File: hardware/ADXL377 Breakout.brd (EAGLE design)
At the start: 17.8 x 17.8 mm, 13 parts, among them U1 ADXL377

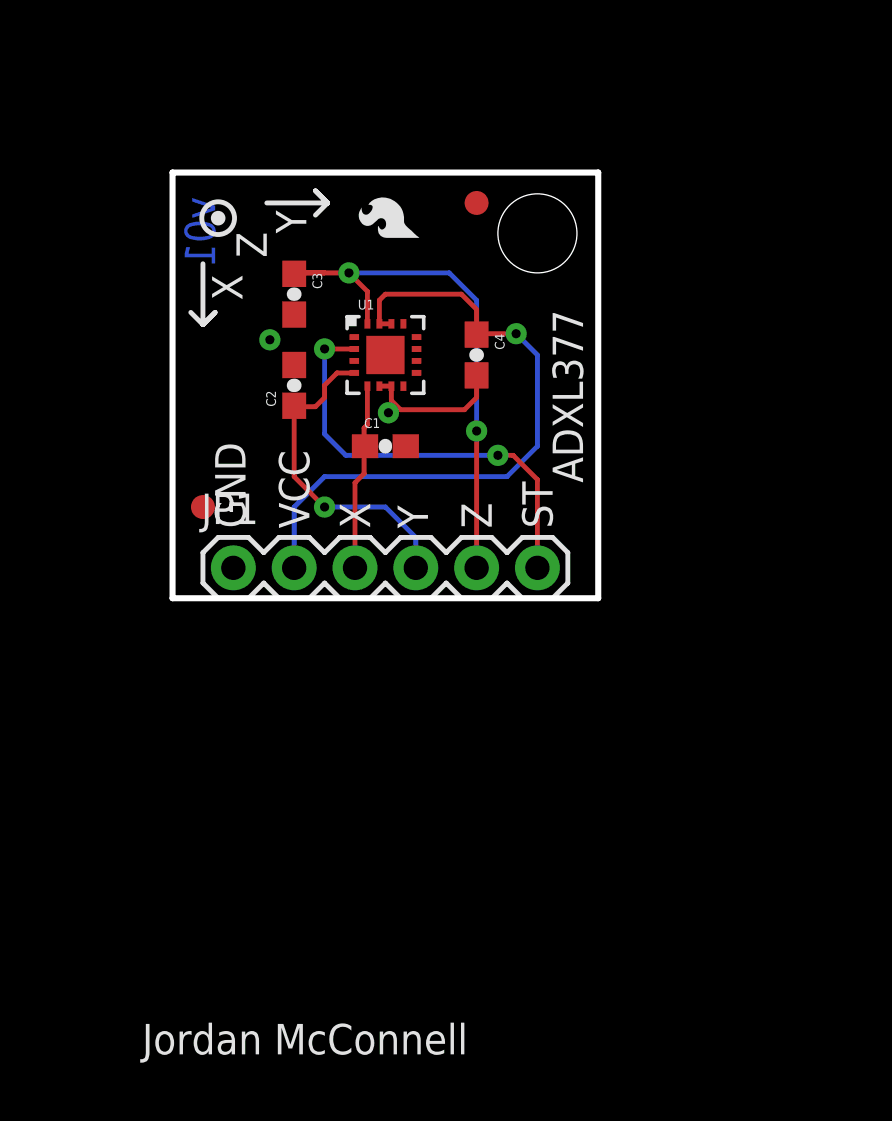
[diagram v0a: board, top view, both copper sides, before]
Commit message: Added 4 mounting holes and modified silk, ready for protos
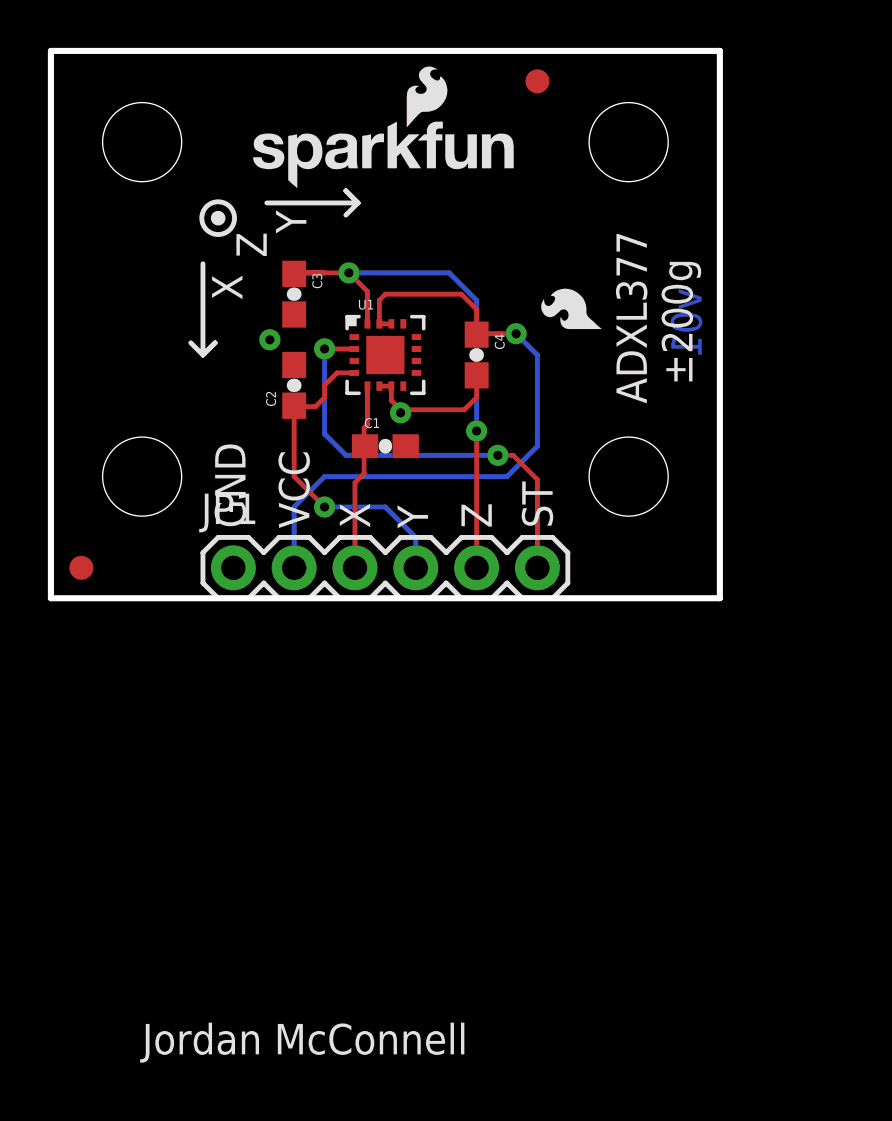
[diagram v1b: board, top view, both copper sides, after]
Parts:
- added LOGO5: SFE_LOGO_NAME_FLAME.1_INCH, SparkFun-Aesthetics:SFE_LOGO_NAME_FLAME_.1
- added STANDOFF2, STANDOFF3, STANDOFF4: STAND-OFF, SparkFun-Electromechanical:STAND-OFF
- moved LOGO1 8.52 mm to (18.3, 10.9)
- moved LOGO3 6.71 mm to (4.32, 17.5)
- moved FID2 5.68 mm to (-3.81, 1.27)
- moved FID1 5.68 mm to (15.2, 21.6)
- moved STANDOFF1 5.39 mm to (19.1, 19.1)
- moved LOGO2 3.59 mm to (17.8, 11.4)
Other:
- board size 17.8 x 17.8 mm -> 27.9 x 22.9 mm
- board text added: "±200g"
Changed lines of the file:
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@@
 <board>
 <plain>
-<wire x1="0" y1="0" x2="17.78" y2="0" width="0.254" layer="20"/>
-<wire x1="17.78" y1="0" x2="17.78" y2="17.78" width="0.254" layer="20"/>
-<wire x1="17.78" y1="17.78" x2="0" y2="17.78" width="0.254" layer="20"/>
-<wire x1="0" y1="17.78" x2="0" y2="0" width="0.254" layer="20"/>
+<wire x1="-5.08" y1="0" x2="22.86" y2="0" width="0.254" layer="20"/>
+<wire x1="22.86" y1="0" x2="22.86" y2="22.86" width="0.254" layer="20"/>
+<wire x1="22.86" y1="22.86" x2="-5.08" y2="22.86" width="0.254" layer="20"/>
+<wire x1="-5.08" y1="22.86" x2="-5.08" y2="0" width="0.254" layer="20"/>
 <circle x="1.905" y="15.875" radius="0.683915625" width="0.2032" layer="21"/>
 <circle x="1.905" y="15.875" radius="0.1524" width="0.3048" layer="21"/>
-<wire x1="3.937" y1="16.51" x2="6.477" y2="16.51" width="0.2032" layer="21"/>
-<wire x1="6.477" y1="16.51" x2="5.969" y2="17.018" width="0.2032" layer="21"/>
-<wire x1="5.969" y1="17.018" x2="6.477" y2="16.51" width="0.2032" layer="21"/>
-<wire x1="6.477" y1="16.51" x2="5.969" y2="16.002" width="0.2032" layer="21"/>
-<wire x1="1.27" y1="13.97" x2="1.27" y2="11.43" width="0.2032" layer="21"/>
-<wire x1="1.27" y1="11.43" x2="1.778" y2="11.938" width="0.2032" layer="21"/>
-<wire x1="1.778" y1="11.938" x2="1.27" y2="11.43" width="0.2032" layer="21"/>
-<wire x1="1.27" y1="11.43" x2="0.762" y2="11.938" width="0.2032" layer="21"/>
+<wire x1="3.937" y1="16.51" x2="7.747" y2="16.51" width="0.2032" layer="21"/>
+<wire x1="7.747" y1="16.51" x2="7.239" y2="17.018" width="0.2032" layer="21"/>
+<wire x1="7.239" y1="17.018" x2="7.747" y2="16.51" width="0.2032" layer="21"/>
+<wire x1="7.747" y1="16.51" x2="7.239" y2="16.002" width="0.2032" layer="21"/>
+<wire x1="1.27" y1="13.97" x2="1.27" y2="10.16" width="0.2032" layer="21"/>
+<wire x1="1.27" y1="10.16" x2="1.778" y2="10.668" width="0.2032" layer="21"/>
+<wire x1="1.778" y1="10.668" x2="1.27" y2="10.16" width="0.2032" layer="21"/>
+<wire x1="1.27" y1="10.16" x2="0.762" y2="10.668" width="0.2032" layer="21"/>
 <text x="3.937" y="14.224" size="1.27" layer="21" font="vector" ratio="15" rot="R90">Z</text>
 <text x="2.921" y="12.446" size="1.27" layer="21" font="vector" ratio="15" rot="R90">X</text>
@@
 <text x="13.335" y="2.921" size="1.27" layer="21" font="vector" ratio="15" rot="R90">Z</text>
 <text x="15.875" y="2.921" size="1.27" layer="21" font="vector" ratio="15" rot="R90">ST</text>
-<text x="17.145" y="4.826" size="1.27" layer="21" font="vector" ratio="15" rot="R90">ADXL377</text>
-<text x="1.778" y="16.764" size="1.27" layer="16" font="vector" ratio="15" rot="SMR270">v01</text>
-<text x="12.319" y="12.827" size="1.27" layer="22" font="vector" ratio="15" rot="SMR270">ADXL377</text>
+<text x="19.812" y="8.128" size="1.27" layer="21" font="vector" ratio="15" rot="R90">ADXL377</text>
+<text x="22.098" y="12.954" size="1.27" layer="16" font="vector" ratio="15" rot="SMR270">v01</text>
+<text x="9.525" y="15.621" size="1.27" layer="22" font="vector" ratio="15" rot="SMR270">ADXL377</text>
 <text x="-1.27" y="-19.05" size="1.27" layer="25" font="vector" ratio="15">Jordan McConnell</text>
+<text x="21.717" y="8.89" size="1.27" layer="21" font="vector" ratio="15" rot="R90">±200g</text>
+<text x="11.303" y="14.224" size="1.27" layer="22" font="vector" ratio="15" rot="SMR270">±200g</text>
 </plain>
 <attributes>
@@
 <attribute name="PROD_ID" value="CAP-00810" x="-5.08" y="-8.89" size="1.778" layer="27" rot="R270" display="off"/>
 </element>
-<element name="FID1" library="SparkFun-Aesthetics" package="FIDUCIAL-1X2" value="FIDUCIAL1X2" x="12.7" y="16.51"/>
-<element name="FID2" library="SparkFun-Aesthetics" package="FIDUCIAL-1X2" value="FIDUCIAL1X2" x="1.27" y="3.81"/>
-<element name="STANDOFF1" library="SparkFun-Electromechanical" package="STAND-OFF" value="STAND-OFF" x="15.24" y="15.24"/>
-<element name="LOGO1" library="SparkFun-Aesthetics" package="SFE_LOGO_FLAME_.1" value="SFE_LOGO_FLAME.1_INCH" x="10.668" y="14.732" rot="R90"/>
-<element name="LOGO2" library="SparkFun-Aesthetics" package="OSHW-LOGO-S" value="OSHW-LOGOS" x="15.24" y="8.89" rot="MR270"/>
-<element name="LOGO3" library="SparkFun-Aesthetics" package="SFE_LOGO_NAME_FLAME_.1" value="SFE_LOGO_NAME_FLAME.1_INCH" x="10.414" y="14.732" rot="MR270"/>
+<element name="FID1" library="SparkFun-Aesthetics" package="FIDUCIAL-1X2" value="FIDUCIAL1X2" x="15.24" y="21.59"/>
+<element name="FID2" library="SparkFun-Aesthetics" package="FIDUCIAL-1X2" value="FIDUCIAL1X2" x="-3.81" y="1.27"/>
+<element name="STANDOFF1" library="SparkFun-Electromechanical" package="STAND-OFF" value="STAND-OFF" x="19.05" y="19.05"/>
+<element name="LOGO1" library="SparkFun-Aesthetics" package="SFE_LOGO_FLAME_.1" value="SFE_LOGO_FLAME.1_INCH" x="18.288" y="10.922" rot="R90"/>
+<element name="LOGO2" library="SparkFun-Aesthetics" package="OSHW-LOGO-S" value="OSHW-LOGOS" x="17.78" y="11.43" rot="MR270"/>
+<element name="LOGO3" library="SparkFun-Aesthetics" package="SFE_LOGO_NAME_FLAME_.1" value="SFE_LOGO_NAME_FLAME.1_INCH" x="4.318" y="17.526" rot="MR270"/>
+<element name="STANDOFF2" library="SparkFun-Electromechanical" package="STAND-OFF" value="STAND-OFF" x="-1.27" y="5.08"/>
+<element name="STANDOFF3" library="SparkFun-Electromechanical" package="STAND-OFF" value="STAND-OFF" x="-1.27" y="19.05"/>
+<element name="STANDOFF4" library="SparkFun-Electromechanical" package="STAND-OFF" value="STAND-OFF" x="19.05" y="5.08"/>
+<element name="LOGO5" library="SparkFun-Aesthetics" package="SFE_LOGO_NAME_FLAME_.1" value="SFE_LOGO_NAME_FLAME.1_INCH" x="2.921" y="17.018"/>
 </elements>
 <signals>
@@
 <wire x1="12.7" y1="8.382" x2="12.7" y2="9.31" width="0.2032" layer="1"/>
 <polygon width="0.2032" layer="16" isolate="0.3048" orphans="yes">
-<vertex x="0" y="17.78"/>
-<vertex x="17.78" y="17.78"/>
-<vertex x="17.78" y="0"/>
-<vertex x="0" y="0"/>
+<vertex x="-5.08" y="22.86"/>
+<vertex x="22.86" y="22.86"/>
+<vertex x="22.86" y="0"/>
+<vertex x="-5.08" y="0"/>
 </polygon>
 <polygon width="0.2032" layer="1" isolate="0.3048" orphans="yes">
-<vertex x="0" y="0"/>
-<vertex x="0" y="17.78"/>
-<vertex x="17.78" y="17.78"/>
-<vertex x="17.78" y="0"/>
+<vertex x="-5.08" y="0"/>
+<vertex x="-5.08" y="22.86"/>
+<vertex x="22.86" y="22.86"/>
+<vertex x="22.86" y="0"/>
 </polygon>
 <via x="4.064" y="10.795" extent="1-16" drill="0.381"/>
-<via x="9.017" y="7.747" extent="1-16" drill="0.381"/>
+<via x="9.525" y="7.747" extent="1-16" drill="0.381"/>
 </signal>
 <signal name="ST">

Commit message: made slight board adjustment, v01 ready for protos
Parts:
- moved FRAME1 7.41 mm to (-5.08, -12.7)
- moved C4 5.08 mm to (17.8, 10.2)
- moved C1 5.08 mm to (14.0, 6.35)
- moved C2 5.08 mm to (10.2, 8.89)
- moved C3 5.08 mm to (10.2, 12.7)
- moved FID1 5.08 mm to (20.3, 21.6)
- moved FID2 5.08 mm to (1.27, 1.27)
- moved JP1 5.08 mm to (7.62, 1.27)
- moved LOGO3 5.08 mm to (9.40, 17.5)
- moved LOGO5 5.08 mm to (8.00, 17.0)
- moved STANDOFF2 5.08 mm to (3.81, 5.08)
- moved STANDOFF3 5.08 mm to (3.81, 19.1)
- moved U1 5.08 mm to (14.0, 10.2)
- moved LOGO1 5.08 mm to (23.4, 10.9)
- moved LOGO2 5.08 mm to (22.9, 11.4)
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
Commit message: v10 ready for review
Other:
- board text added: "3.3V"
- board text added: "v10"
- board text removed: "VCC"
- board text removed: "v01"
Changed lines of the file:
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@@
 <text x="10.668" y="15.24" size="1.27" layer="21" font="vector" ratio="15" rot="R90">Y</text>
 <text x="8.128" y="2.921" size="1.27" layer="21" font="vector" ratio="15" rot="R90">GND</text>
-<text x="10.795" y="2.921" size="1.27" layer="21" font="vector" ratio="15" rot="R90">VCC</text>
+<text x="10.795" y="2.921" size="1.27" layer="21" font="vector" ratio="15" rot="R90">3.3V</text>
 <text x="13.335" y="2.921" size="1.27" layer="21" font="vector" ratio="15" rot="R90">X</text>
 <text x="15.748" y="2.921" size="1.27" layer="21" font="vector" ratio="15" rot="R90">Y</text>
@@
 <text x="20.955" y="2.921" size="1.27" layer="21" font="vector" ratio="15" rot="R90">ST</text>
 <text x="24.892" y="8.128" size="1.27" layer="21" font="vector" ratio="15" rot="R90">ADXL377</text>
-<text x="27.178" y="12.954" size="1.27" layer="16" font="vector" ratio="15" rot="SMR270">v01</text>
+<text x="27.178" y="12.954" size="1.27" layer="16" font="vector" ratio="15" rot="SMR270">v10</text>
 <text x="14.605" y="15.621" size="1.27" layer="22" font="vector" ratio="15" rot="SMR270">ADXL377</text>
 <text x="5.08" y="-15.24" size="1.27" layer="25" font="vector" ratio="15">Jordan McConnell</text>

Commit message: v10, ready for reds
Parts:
- removed LOGO5: SFE_LOGO_NAME_FLAME.1_INCH, SparkFun-Aesthetics:SFE_LOGO_NAME_FLAME_.1
- moved LOGO1 18.9 mm to (4.57, 9.14)
- moved LOGO3 9.21 mm to (18.3, 15.1)
- moved FID1 6.35 mm to (16.5, 16.5)
- moved STANDOFF1 5.39 mm to (20.3, 15.2)
- moved STANDOFF3 4.02 mm to (2.54, 15.2)
- moved STANDOFF4 3.81 mm to (20.3, 5.08)
- moved LOGO2 2.84 mm to (20.3, 10.2)
- moved C1 2.54 mm to (11.4, 6.35)
- moved C4 2.54 mm to (15.2, 10.2)
- moved U1 2.54 mm to (11.4, 10.2)
- moved C2 2.54 mm to (7.62, 8.89)
- moved C3 2.54 mm to (7.62, 12.7)
- moved JP1 2.54 mm to (5.08, 1.27)
- moved STANDOFF2 1.27 mm to (2.54, 5.08)
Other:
- board size 27.9 x 22.9 mm -> 22.9 x 17.8 mm
